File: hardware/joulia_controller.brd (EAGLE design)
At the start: 121 x 68 mm, 44 parts, among them IC1 LM2902D, IC2 LM2902D, U1 MMBT2222ALT1G, U2 MMBT2222ALT1G

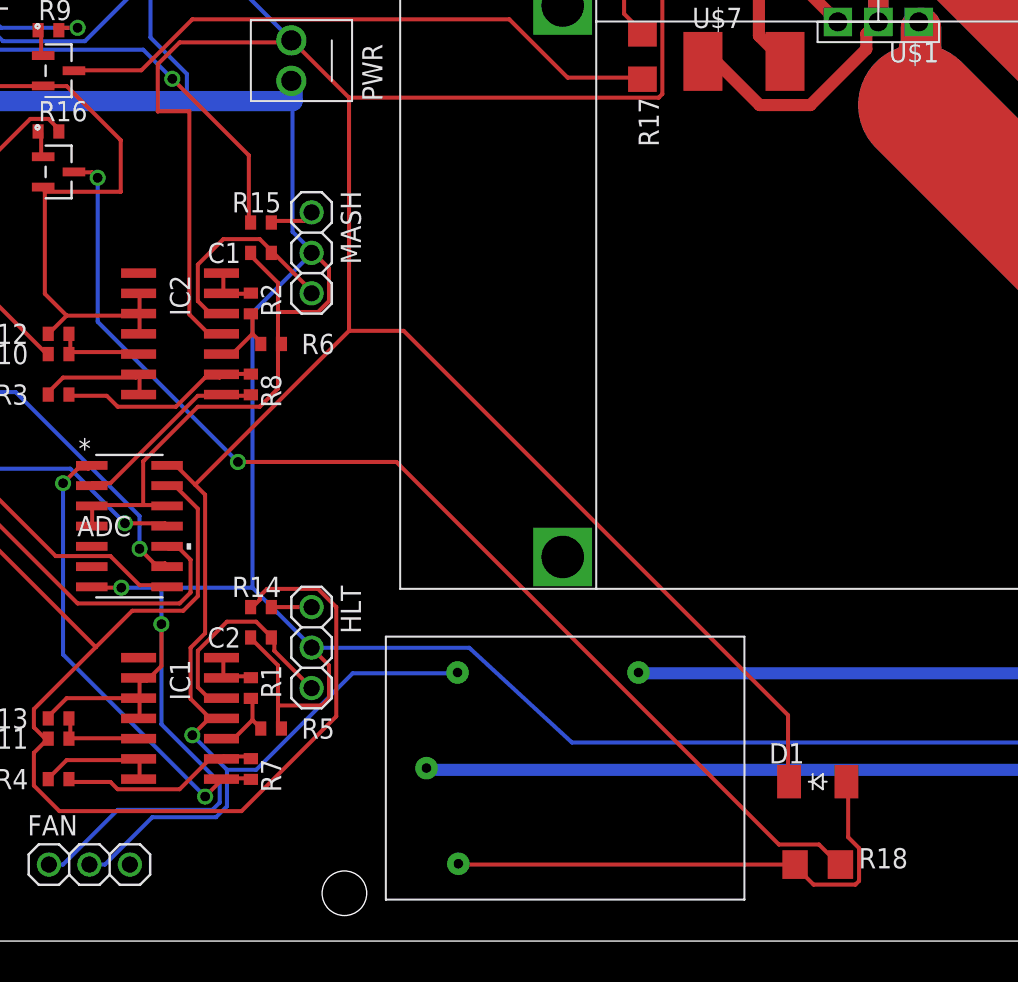
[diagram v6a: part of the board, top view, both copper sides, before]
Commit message: Removing extraneous resistor for relay.
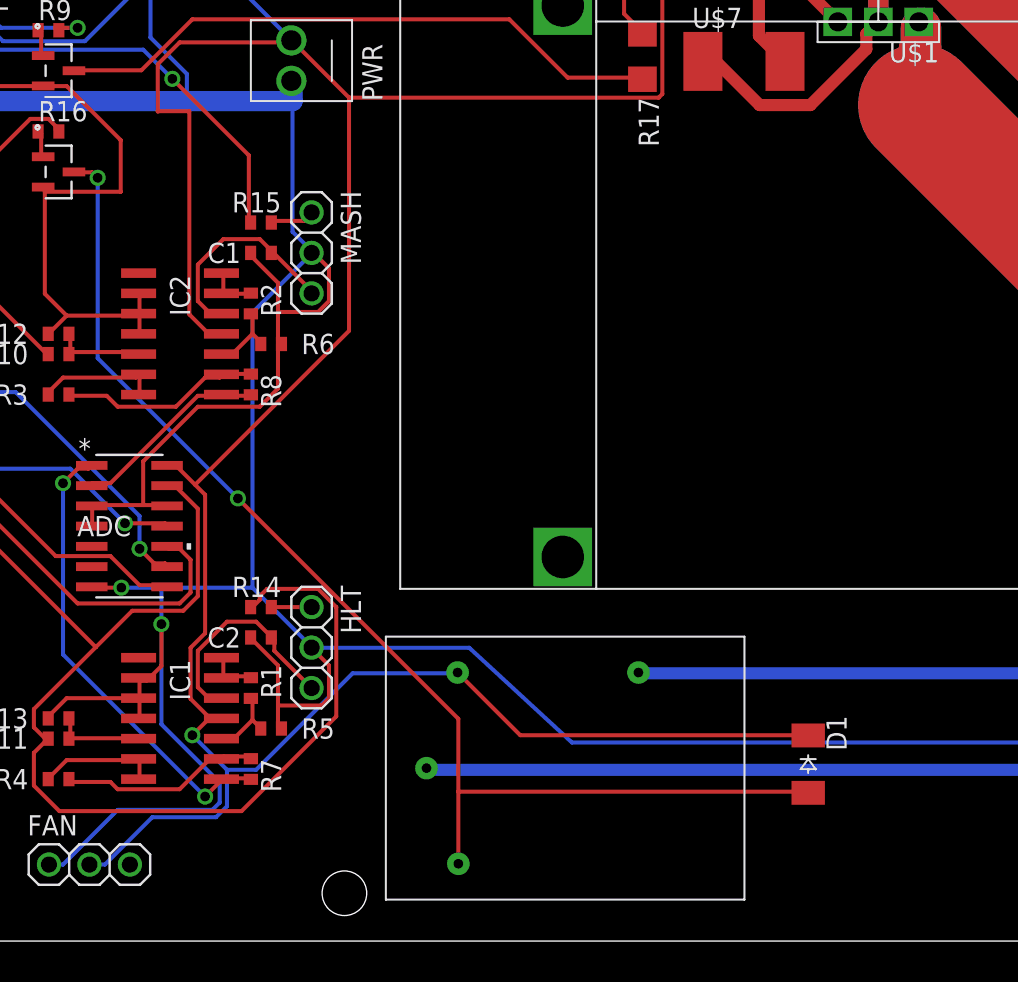
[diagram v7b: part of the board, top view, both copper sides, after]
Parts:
- removed R18: 330, resistor:R1206
- moved D1 1.25 mm to (59.1, 11.1), turned to 270 degrees
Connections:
- removed net N$17: D1.A, R18.2, U$3.P$2
- net N$18: now also D1.A, U$3.P$2; no longer R18.1
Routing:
- net N$17: track 32.4 -> 0.00 mm
- net +5V: track 222.5 -> 204.4 mm
- net N$18: track 71.4 -> 76.1 mm
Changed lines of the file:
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@@
 <attribute name="NAME" x="49.73" y="52.93" size="1.27" layer="25" rot="R90" align="bottom-right"/>
-</element>
-<element name="R18" library="resistor" library_urn="urn:adsk.eagle:library:348" package="R1206" value="330" x="59.7" y="4.8" smashed="yes" rot="R180">
-<attribute name="NAME" x="62.27" y="5.83" size="1.27" layer="25" rot="R180" align="bottom-right"/>
 </element>
 <element name="HELED" library="eagle-ltspice" library_urn="urn:adsk.eagle:library:217" package="LED_SML0603" value="" x="11.6" y="65.2">
@@
 <element name="U$3" library="digikey" package="G5LE-1A4_DC5" value="G5LE-1A4_DC5" x="32.6" y="2.6" rot="R90"/>
 <element name="U$2" library="digikey" package="VM2-038-1AE" value="VM1-038-1AEHORIZONTAL" x="33.5" y="60.7"/>
-<element name="D1" library="diode" library_urn="urn:adsk.eagle:library:210" package="SOD-123_MINI-SMA" value="CGRM4001-G" x="59.7" y="10"/>
+<element name="D1" library="diode" library_urn="urn:adsk.eagle:library:210" package="SOD-123_MINI-SMA" value="CGRM4001-G" x="59.1" y="11.1" rot="R270"/>
 </elements>
 <signals>
@@
 <wire x1="20.2692" y1="52.07" x2="20.2692" y2="39.3192" width="0.254" layer="1"/>
 <contactref element="U$5" pad="P$6"/>
-<wire x1="19.431" y1="29.8323" x2="18.9738" y2="29.8323" width="0.254" layer="1"/>
-<wire x1="21.2598" y1="28.0035" x2="20.63115" y2="28.63215" width="0.254" layer="1"/>
-<wire x1="20.63115" y1="28.63215" x2="19.431" y2="29.8323" width="0.254" layer="1"/>
-<wire x1="21.2598" y1="19.3167" x2="21.2598" y2="28.0035" width="0.254" layer="1"/>
-<wire x1="20.3454" y1="18.4023" x2="21.2598" y2="19.3167" width="0.254" layer="1"/>
-<wire x1="20.3454" y1="15.2019" x2="20.3454" y2="18.4023" width="0.254" layer="1"/>
-<wire x1="21.4884" y1="14.0589" x2="20.3454" y2="15.2019" width="0.254" layer="1"/>
-<wire x1="22.1742" y1="14.0589" x2="21.4884" y2="14.0589" width="0.254" layer="1"/>
-<wire x1="18.9738" y1="29.8323" x2="18.8722" y2="29.845" width="0.254" layer="1"/>
-<wire x1="22.1742" y1="14.0589" x2="22.285" y2="13.97" width="0.254" layer="1"/>
 <contactref element="FAN" pad="2"/>
 <wire x1="14.9733" y1="4.8006" x2="14.0589" y2="4.8006" width="0.254" layer="16"/>
@@
 <wire x1="22.6314" y1="10.7442" x2="24.4602" y2="10.7442" width="0.254" layer="16"/>
 <wire x1="37.0332" y1="16.8021" x2="37.1" y2="16.85" width="0.254" layer="16"/>
-<wire x1="48.8061" y1="65.0367" x2="48.8061" y2="65.7225" width="0.254" layer="1"/>
-<wire x1="49.9491" y1="63.8937" x2="48.8061" y2="65.0367" width="0.254" layer="1"/>
-<wire x1="49.9491" y1="53.1495" x2="49.9491" y2="63.8937" width="0.254" layer="1"/>
-<wire x1="49.7205" y1="52.9209" x2="49.9491" y2="53.1495" width="0.254" layer="1"/>
-<wire x1="30.2895" y1="52.9209" x2="49.7205" y2="52.9209" width="0.254" layer="1"/>
-<wire x1="26.7462" y1="56.4642" x2="30.2895" y2="52.9209" width="0.254" layer="1"/>
-<wire x1="48.8061" y1="65.7225" x2="48.7" y2="65.795" width="0.254" layer="1"/>
-<wire x1="26.7462" y1="56.4642" x2="26.67" y2="56.515" width="0.254" layer="1"/>
 <wire x1="6.6294" y1="58.4073" x2="5.715" y2="58.4073" width="0.254" layer="16"/>
 <wire x1="8.5725" y1="56.4642" x2="6.6294" y2="58.4073" width="0.254" layer="16"/>
@@
 <wire x1="5.715" y1="58.4073" x2="5.715" y2="58.42" width="0.254" layer="16"/>
 <wire x1="26.6319" y1="56.5785" x2="26.67" y2="56.515" width="0.254" layer="16"/>
-<wire x1="30.2895" y1="38.2905" x2="20.63115" y2="28.63215" width="0.254" layer="1"/>
-<wire x1="30.2895" y1="52.9209" x2="30.2895" y2="38.2905" width="0.254" layer="1"/>
 <contactref element="D1" pad="C"/>
-<wire x1="57.8358" y1="14.1732" x2="57.8358" y2="10.0584" width="0.254" layer="1"/>
-<wire x1="33.7185" y1="38.2905" x2="57.8358" y2="14.1732" width="0.254" layer="1"/>
-<wire x1="30.2895" y1="38.2905" x2="33.7185" y2="38.2905" width="0.254" layer="1"/>
-<wire x1="57.8358" y1="10.0584" x2="57.9" y2="10" width="0.254" layer="1"/>
+<wire x1="48.8061" y1="65.0367" x2="48.8061" y2="65.7225" width="0.254" layer="1"/>
+<wire x1="49.9491" y1="63.8937" x2="48.8061" y2="65.0367" width="0.254" layer="1"/>
+<wire x1="49.9491" y1="53.1495" x2="49.9491" y2="63.8937" width="0.254" layer="1"/>
+<wire x1="49.7205" y1="52.9209" x2="49.9491" y2="53.1495" width="0.254" layer="1"/>
+<wire x1="30.2895" y1="52.9209" x2="49.7205" y2="52.9209" width="0.254" layer="1"/>
+<wire x1="26.7462" y1="56.4642" x2="30.2895" y2="52.9209" width="0.254" layer="1"/>
+<wire x1="48.8061" y1="65.7225" x2="48.7" y2="65.795" width="0.254" layer="1"/>
+<wire x1="26.7462" y1="56.4642" x2="26.67" y2="56.515" width="0.254" layer="1"/>
+<wire x1="19.431" y1="29.8323" x2="18.9738" y2="29.8323" width="0.254" layer="1"/>
+<wire x1="21.2598" y1="28.0035" x2="20.63115" y2="28.63215" width="0.254" layer="1"/>
+<wire x1="20.63115" y1="28.63215" x2="19.431" y2="29.8323" width="0.254" layer="1"/>
+<wire x1="21.2598" y1="19.3167" x2="21.2598" y2="28.0035" width="0.254" layer="1"/>
+<wire x1="20.3454" y1="18.4023" x2="21.2598" y2="19.3167" width="0.254" layer="1"/>
+<wire x1="20.3454" y1="15.2019" x2="20.3454" y2="18.4023" width="0.254" layer="1"/>
+<wire x1="21.4884" y1="14.0589" x2="20.3454" y2="15.2019" width="0.254" layer="1"/>
+<wire x1="18.9738" y1="29.8323" x2="18.8722" y2="29.845" width="0.254" layer="1"/>
+<wire x1="21.4884" y1="14.0589" x2="22.285" y2="13.97" width="0.254" layer="1"/>
+<wire x1="41.0337" y1="12.9159" x2="59.0931" y2="12.9159" width="0.254" layer="1"/>
+<wire x1="37.1475" y1="16.8021" x2="41.0337" y2="12.9159" width="0.254" layer="1"/>
+<wire x1="59.0931" y1="12.9159" x2="59.1" y2="12.9" width="0.254" layer="1"/>
+<wire x1="37.1475" y1="16.8021" x2="37.1" y2="16.85" width="0.254" layer="1"/>
+<wire x1="30.2895" y1="38.2905" x2="30.2895" y2="52.9209" width="0.254" layer="1"/>
+<wire x1="20.63115" y1="28.63215" x2="30.2895" y2="38.2905" width="0.254" layer="1"/>
 </signal>
 <signal name="+3V3">
@@
 <wire x1="48.6918" y1="57.0357" x2="48.7" y2="56.922" width="0.254" layer="1"/>
 </signal>
-<signal name="N$17">
-<contactref element="R18" pad="2"/>
-<contactref element="U$3" pad="P$2"/>
-<wire x1="37.2618" y1="4.8006" x2="58.1787" y2="4.8006" width="0.254" layer="1"/>
-<wire x1="58.1787" y1="4.8006" x2="58.278" y2="4.8" width="0.254" layer="1"/>
-<wire x1="37.2618" y1="4.8006" x2="37.15" y2="4.85" width="0.254" layer="1"/>
-<contactref element="D1" pad="A"/>
-<wire x1="61.6077" y1="6.5151" x2="61.6077" y2="9.9441" width="0.254" layer="1"/>
-<wire x1="62.2935" y1="5.8293" x2="61.6077" y2="6.5151" width="0.254" layer="1"/>
-<wire x1="62.2935" y1="3.7719" x2="62.2935" y2="5.8293" width="0.254" layer="1"/>
-<wire x1="62.0649" y1="3.5433" x2="62.2935" y2="3.7719" width="0.254" layer="1"/>
-<wire x1="59.436" y1="3.5433" x2="62.0649" y2="3.5433" width="0.254" layer="1"/>
-<wire x1="58.293" y1="4.6863" x2="59.436" y2="3.5433" width="0.254" layer="1"/>
-<wire x1="61.6077" y1="9.9441" x2="61.5" y2="10" width="0.254" layer="1"/>
-<wire x1="58.293" y1="4.6863" x2="58.278" y2="4.8" width="0.254" layer="1"/>
-</signal>
 <signal name="N$18">
 <contactref element="U2" pad="3"/>
-<contactref element="R18" pad="1"/>
+<contactref element="U$3" pad="P$2"/>
+<contactref element="D1" pad="A"/>
 <wire x1="14.1732" y1="48.2346" x2="13.0302" y2="48.2346" width="0.254" layer="1"/>
 <wire x1="14.5161" y1="47.8917" x2="14.1732" y2="48.2346" width="0.254" layer="1"/>
-<wire x1="14.5161" y1="38.862" x2="14.5161" y2="47.8917" width="0.254" layer="16"/>
-<wire x1="23.3172" y1="30.0609" x2="14.5161" y2="38.862" width="0.254" layer="16"/>
-<wire x1="33.2613" y1="30.0609" x2="23.3172" y2="30.0609" width="0.254" layer="1"/>
-<wire x1="57.2643" y1="6.0579" x2="33.2613" y2="30.0609" width="0.254" layer="1"/>
-<wire x1="59.7789" y1="6.0579" x2="57.2643" y2="6.0579" width="0.254" layer="1"/>
-<wire x1="61.0362" y1="4.8006" x2="59.7789" y2="6.0579" width="0.254" layer="1"/>
+<wire x1="14.5161" y1="36.576" x2="14.5161" y2="47.8917" width="0.254" layer="16"/>
+<wire x1="23.3172" y1="27.7749" x2="14.5161" y2="36.576" width="0.254" layer="16"/>
+<wire x1="37.1475" y1="13.9446" x2="23.3172" y2="27.7749" width="0.254" layer="1"/>
+<wire x1="37.1475" y1="4.9149" x2="37.1475" y2="9.3726" width="0.254" layer="1"/>
+<wire x1="37.1475" y1="9.3726" x2="37.1475" y2="13.9446" width="0.254" layer="1"/>
 <wire x1="13.0302" y1="48.2346" x2="13.0302" y2="48.26" width="0.254" layer="1"/>
-<wire x1="61.0362" y1="4.8006" x2="61.122" y2="4.8" width="0.254" layer="1"/>
+<wire x1="37.1475" y1="4.9149" x2="37.15" y2="4.85" width="0.254" layer="1"/>
+<wire x1="37.1475" y1="9.3726" x2="59.0931" y2="9.3726" width="0.254" layer="1"/>
+<wire x1="59.0931" y1="9.3726" x2="59.1" y2="9.3" width="0.254" layer="1"/>
 <via x="14.5161" y="47.8917" extent="1-16" drill="0.6096"/>
-<via x="23.3172" y="30.0609" extent="1-16" drill="0.6096"/>
+<via x="23.3172" y="27.7749" extent="1-16" drill="0.6096"/>
 </signal>
 <signal name="-120" class="2">

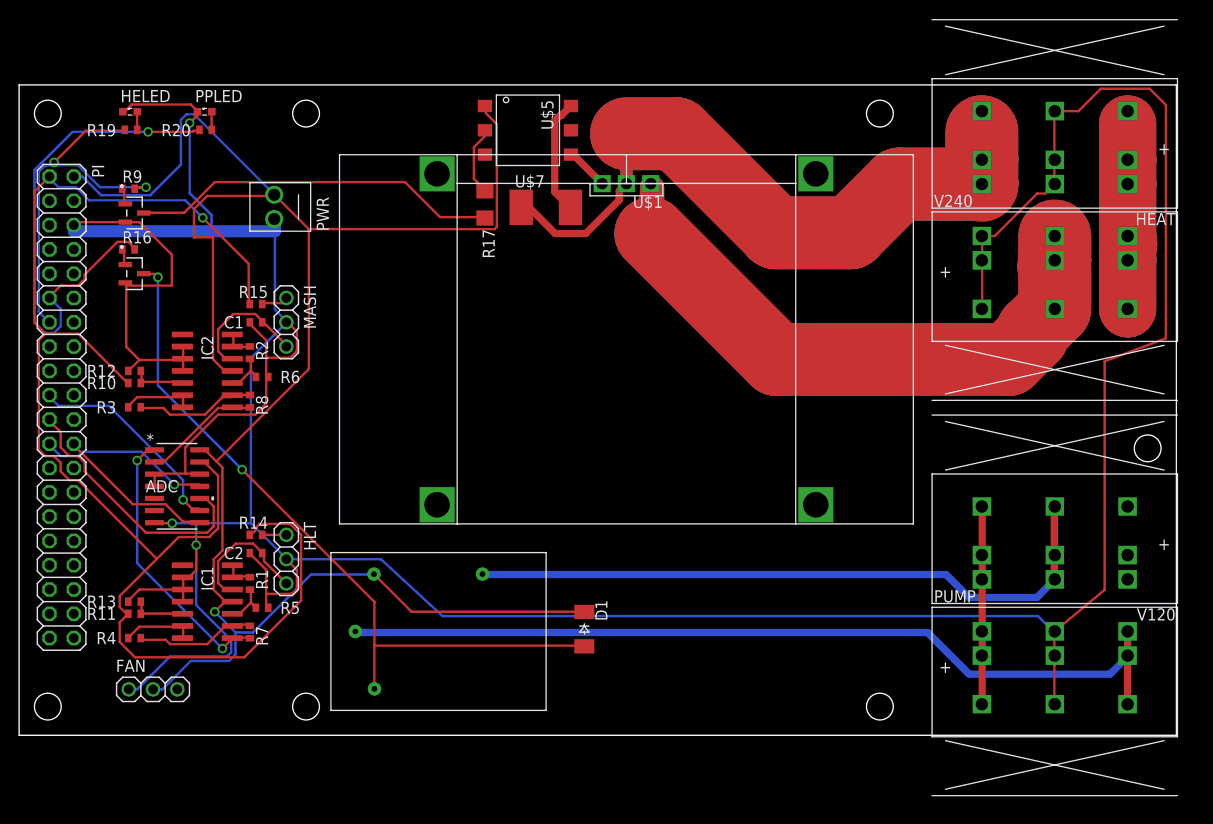
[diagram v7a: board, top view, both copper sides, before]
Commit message: Switches two plugs for one board terminal for 120V connections.
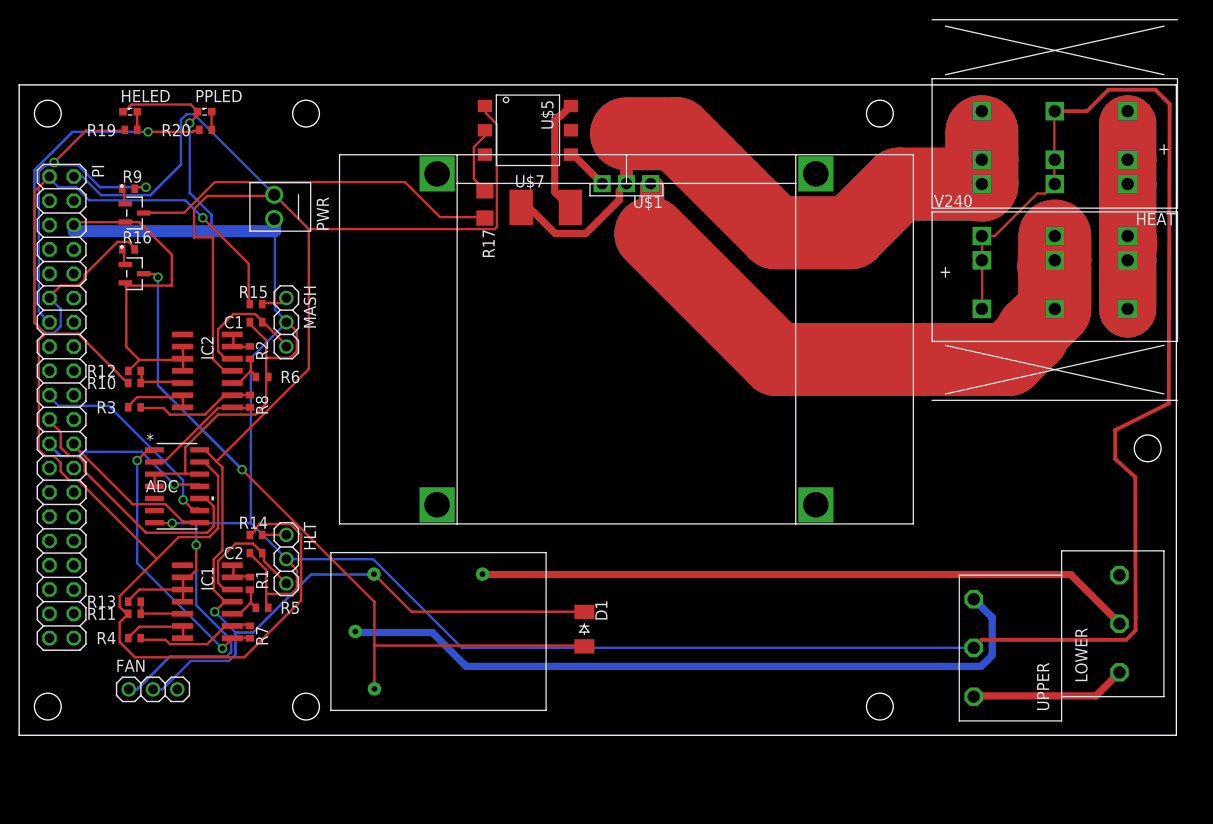
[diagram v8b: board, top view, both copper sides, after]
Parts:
- removed PUMP, V120: PC1720589, digikey:PC-PCV5/3-G-7.62
- added U$4: PC1725041, digikey:PC-MKKDS1.5/3-5.08
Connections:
- net 120H: now also U$4.P$2; no longer V120.P$1, V120.P$2, V120.P$3
- net 120N: now also U$4.P$1, U$4.P$4; no longer PUMP.P$7, PUMP.P$8, PUMP.P$9, V120.P$4, V120.P$5, V120.P$6
- net GND: now also U$4.P$5; no longer PUMP.P$1, PUMP.P$2, PUMP.P$3
- net N$24: now also U$4.P$6; no longer PUMP.P$4, PUMP.P$5, PUMP.P$6
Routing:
- net N$24: track 91.2 -> 75.3 mm
- net 120N: track 20.8 -> 16.3 mm
- net GND: track 415.4 -> 413.7 mm
- net 120H: track 69.3 -> 68.8 mm
